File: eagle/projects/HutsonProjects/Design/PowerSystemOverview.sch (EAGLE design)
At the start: 28 parts, among them U1 MCP7384XX, U3 MT3608, U4 LTC3531ES6-3_3

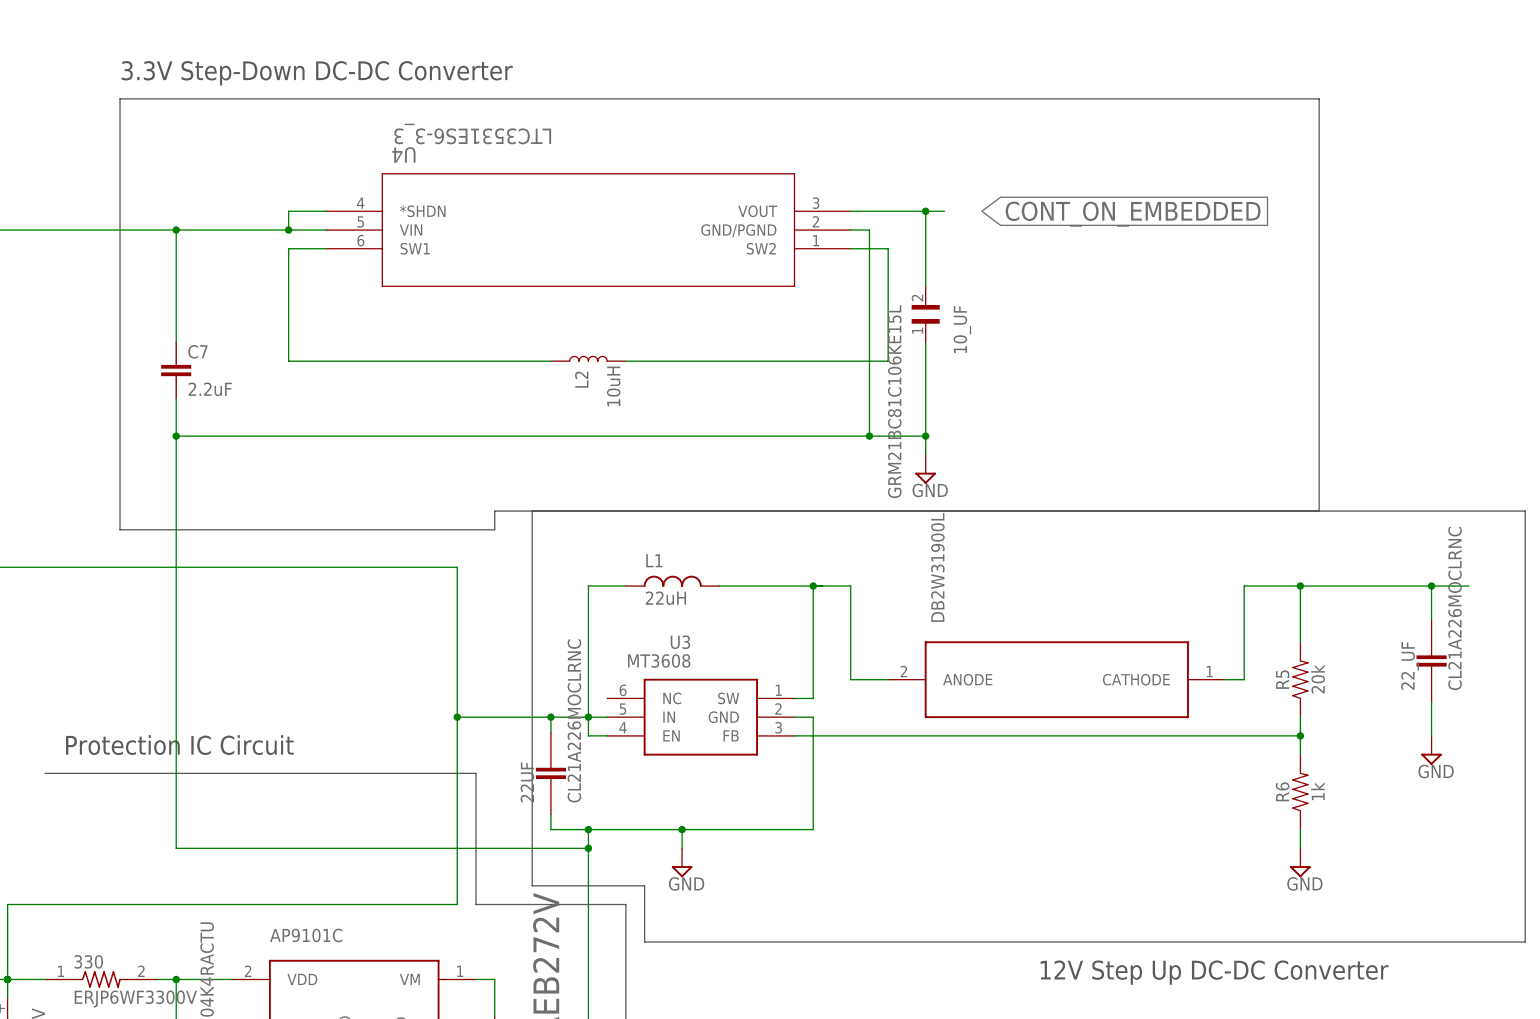
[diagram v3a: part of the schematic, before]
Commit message: 2.2 uF capacitor chip added
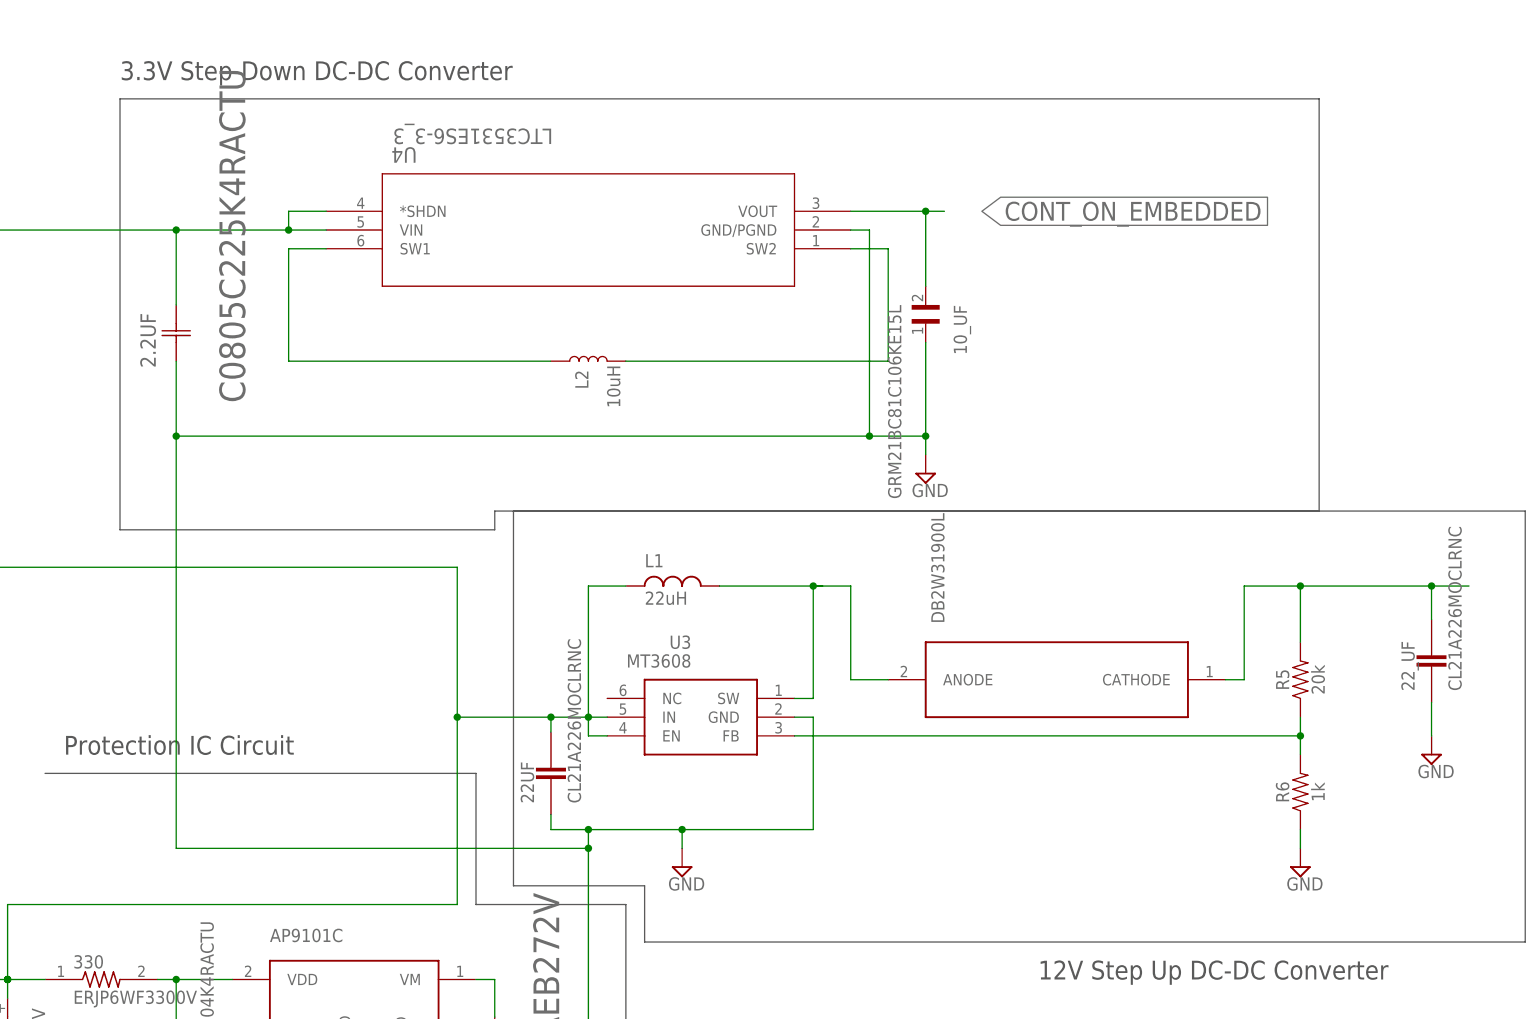
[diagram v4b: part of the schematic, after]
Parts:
- removed C7: 2.2uF, SparkFun-Capacitors:2.2UF-0603-10V-20%
- added 2.2UF: C0805C225K4RACTU, C0805C225K4RACTU:C0805C225K4RACTU
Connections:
- net GND: now also 2.2UF.C1; no longer C7.2
- net N$16: now also 2.2UF.C2; no longer C7.1
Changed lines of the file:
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@@
 <part name="U4" library="LTC3531ES6-3_3" deviceset="LTC3531ES6-3_3" device=""/>
 <part name="L2" library="SparkFun-Coils" deviceset="INDUCTOR" device="INDUCTOR_10UH" value="10uH"/>
-<part name="C7" library="SparkFun-Capacitors" deviceset="2.2UF" device="-0603-10V-20%" value="2.2uF"/>
 <part name="U$4" library="AP910C" deviceset="AP9101C" device=""/>
 <part name="U$5" library="DB2W31900L" deviceset="DB2W31900" device=""/>
@@
 <part name="22_UF" library="CL21A226MOCLRNC" deviceset="CL21A226MOCLRNC" device=""/>
 <part name="SUPPLY7" library="supply2" library_urn="urn:adsk.eagle:library:372" deviceset="GND" device=""/>
+<part name="2.2UF" library="C0805C225K4RACTU" deviceset="C0805C225K4RACTU" device=""/>
 </parts>
 <sheets>
@@
 <attribute name="VALUE" x="170.18" y="189.23" size="1.778" layer="96" font="vector" rot="R90" align="top-left"/>
 </instance>
-<instance part="C7" gate="G$1" x="111.76" y="193.04" smashed="yes">
-<attribute name="NAME" x="113.284" y="195.961" size="1.778" layer="95" font="vector"/>
-<attribute name="VALUE" x="113.284" y="190.881" size="1.778" layer="96" font="vector"/>
-</instance>
 <instance part="U$4" gate="G$1" x="137.16" y="109.22" smashed="yes">
 <attribute name="VALUE" x="124.46" y="99.06" size="1.778" layer="96"/>
@@
 <attribute name="VALUE" x="280.035" y="139.065" size="1.778" layer="96"/>
 </instance>
+<instance part="2.2UF" gate="A" x="111.76" y="195.58" smashed="yes" rot="R90">
+<attribute name="VALUE" x="121.109640625" y="189.91431875" size="3.480709375" layer="96" ratio="10" rot="SR90"/>
+<attribute name="NAME" x="108.99125" y="194.66555" size="2.082909375" layer="95" ratio="10" rot="SR90"/>
+</instance>
 </instances>
 <busses>
@@
 <bus name="N$18">
 <segment>
-<wire x1="160.02" y1="175.26" x2="160.02" y2="124.46" width="0.508" layer="92"/>
-<wire x1="160.02" y1="124.46" x2="175.26" y2="124.46" width="0.508" layer="92"/>
+<wire x1="157.48" y1="175.26" x2="157.48" y2="124.46" width="0.508" layer="92"/>
+<wire x1="157.48" y1="124.46" x2="175.26" y2="124.46" width="0.508" layer="92"/>
 <wire x1="175.26" y1="124.46" x2="175.26" y2="116.84" width="0.508" layer="92"/>
 <wire x1="175.26" y1="116.84" x2="294.64" y2="116.84" width="0.508" layer="92"/>
 <wire x1="294.64" y1="116.84" x2="294.64" y2="175.26" width="0.508" layer="92"/>
-<wire x1="294.64" y1="175.26" x2="160.02" y2="175.26" width="0.508" layer="92"/>
+<wire x1="294.64" y1="175.26" x2="157.48" y2="175.26" width="0.508" layer="92"/>
 </segment>
 </bus>
@@
 <wire x1="167.64" y1="129.54" x2="111.76" y2="129.54" width="0.1524" layer="91"/>
 <pinref part="SUPPLY14" gate="GND" pin="GND"/>
-<pinref part="C7" gate="G$1" pin="2"/>
 <wire x1="213.36" y1="185.42" x2="213.36" y2="182.88" width="0.1524" layer="91"/>
-<wire x1="111.76" y1="190.5" x2="111.76" y2="185.42" width="0.1524" layer="91"/>
 <wire x1="111.76" y1="185.42" x2="205.74" y2="185.42" width="0.1524" layer="91"/>
 <pinref part="U4" gate="A" pin="GND/PGND"/>
@@
 <junction x="205.74" y="185.42"/>
 <wire x1="111.76" y1="129.54" x2="111.76" y2="185.42" width="0.1524" layer="91"/>
-<junction x="111.76" y="185.42"/>
 <junction x="167.64" y="129.54"/>
 <pinref part="2.7K" gate="A" pin="R2"/>
@@
 <pinref part="22UF" gate="G$1" pin="1"/>
 <wire x1="162.56" y1="134.112" x2="162.56" y2="132.08" width="0.1524" layer="91"/>
+<pinref part="2.2UF" gate="A" pin="C1"/>
+<wire x1="111.76" y1="195.58" x2="111.76" y2="185.42" width="0.1524" layer="91"/>
+<junction x="111.76" y="185.42"/>
 </segment>
 <segment>
@@
 <wire x1="149.86" y1="167.64" x2="83.82" y2="167.64" width="0.1524" layer="91"/>
 <junction x="149.86" y="147.32"/>
-<pinref part="C7" gate="G$1" pin="1"/>
 <pinref part="U4" gate="A" pin="VIN"/>
 <wire x1="127" y1="213.36" x2="132.08" y2="213.36" width="0.1524" layer="91"/>
@@
 <wire x1="127" y1="215.9" x2="127" y2="213.36" width="0.1524" layer="91"/>
 <junction x="127" y="213.36"/>
-<wire x1="111.76" y1="213.36" x2="127" y2="213.36" width="0.1524" layer="91"/>
-<wire x1="111.76" y1="213.36" x2="111.76" y2="198.12" width="0.1524" layer="91"/>
 <wire x1="83.82" y1="167.64" x2="83.82" y2="213.36" width="0.1524" layer="91"/>
 <wire x1="83.82" y1="213.36" x2="111.76" y2="213.36" width="0.1524" layer="91"/>
-<junction x="111.76" y="213.36"/>
 <pinref part="330" gate="G$1" pin="1"/>
+<wire x1="111.76" y1="213.36" x2="127" y2="213.36" width="0.1524" layer="91"/>
 <wire x1="88.9" y1="111.76" x2="93.98" y2="111.76" width="0.1524" layer="91"/>
 <junction x="88.9" y="111.76"/>
@@
 <wire x1="162.56" y1="147.32" x2="162.56" y2="145.288" width="0.1524" layer="91"/>
 <junction x="162.56" y="147.32"/>
-</segment>
-</net>
+<pinref part="2.2UF" gate="A" pin="C2"/>
+<wire x1="111.76" y1="213.36" x2="111.76" y2="203.2" width="0.1524" layer="91"/>
+<junction x="111.76" y="213.36"/>
+</segment>
+</net>

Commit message: Deleted Outlines for circuit optimization
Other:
- note removed: "12V Step Up DC-DC Converter"
- note removed: "3.3V Step-Down DC-DC Converter"
- note removed: "Charging Circuit"
- note removed: "Protection IC Circuit"
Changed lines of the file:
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@@
 <plain>
 <text x="45.72" y="121.92" size="1.778" layer="91">NDS8434 P-Channel </text>
-<text x="-38.1" y="149.86" size="2.54" layer="92">Charging Circuit</text>
-<text x="96.52" y="142.24" size="2.54" layer="92">Protection IC Circuit</text>
-<text x="228.6" y="111.76" size="2.54" layer="92">12V Step Up DC-DC Converter</text>
-<text x="104.14" y="233.68" size="2.54" layer="92">3.3V Step-Down DC-DC Converter</text>
 <text x="190.5" y="81.28" size="2.54" layer="94">Power Distribution Circuit</text>
 <text x="210.82" y="71.12" size="2.54" layer="94">DWG-001</text>
@@
 </instances>
 <busses>
-<bus name="B$1">
-<segment>
-<wire x1="-106.68" y1="147.32" x2="83.82" y2="147.32" width="0.508" layer="92"/>
-<wire x1="83.82" y1="147.32" x2="83.82" y2="60.96" width="0.508" layer="92"/>
-<wire x1="83.82" y1="60.96" x2="-106.68" y2="60.96" width="0.508" layer="92"/>
-<wire x1="-106.68" y1="60.96" x2="-106.68" y2="147.32" width="0.508" layer="92"/>
-</segment>
-</bus>
-<bus name="B$2">
-<segment>
-<wire x1="93.98" y1="60.96" x2="172.72" y2="60.96" width="0.508" layer="92"/>
-<wire x1="172.72" y1="60.96" x2="172.72" y2="121.92" width="0.508" layer="92"/>
-<wire x1="172.72" y1="121.92" x2="152.4" y2="121.92" width="0.508" layer="92"/>
-<wire x1="152.4" y1="121.92" x2="152.4" y2="139.7" width="0.508" layer="92"/>
-<wire x1="152.4" y1="139.7" x2="93.98" y2="139.7" width="0.508" layer="92"/>
-</segment>
-</bus>
-<bus name="N$18">
-<segment>
-<wire x1="157.48" y1="175.26" x2="157.48" y2="124.46" width="0.508" layer="92"/>
-<wire x1="157.48" y1="124.46" x2="175.26" y2="124.46" width="0.508" layer="92"/>
-<wire x1="175.26" y1="124.46" x2="175.26" y2="116.84" width="0.508" layer="92"/>
-<wire x1="175.26" y1="116.84" x2="294.64" y2="116.84" width="0.508" layer="92"/>
-<wire x1="294.64" y1="116.84" x2="294.64" y2="175.26" width="0.508" layer="92"/>
-<wire x1="294.64" y1="175.26" x2="157.48" y2="175.26" width="0.508" layer="92"/>
-</segment>
-</bus>
-<bus name="B$4">
-<segment>
-<wire x1="104.14" y1="231.14" x2="104.14" y2="172.72" width="0.508" layer="92"/>
-<wire x1="104.14" y1="172.72" x2="154.94" y2="172.72" width="0.508" layer="92"/>
-<wire x1="154.94" y1="172.72" x2="154.94" y2="175.26" width="0.508" layer="92"/>
-<wire x1="154.94" y1="175.26" x2="266.7" y2="175.26" width="0.508" layer="92"/>
-<wire x1="266.7" y1="175.26" x2="266.7" y2="231.14" width="0.508" layer="92"/>
-<wire x1="266.7" y1="231.14" x2="104.14" y2="231.14" width="0.508" layer="92"/>
-</segment>
-</bus>
 </busses>
 <nets>
